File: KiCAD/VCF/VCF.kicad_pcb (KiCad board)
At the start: 2 copper layers, 50 x 100 mm, 50 parts, among them J1 FM, J2 CV, J3 IN, J4 OUT, J5 Conn_01x03, J6 Conn_01x03, Q1 2N3904, SW1 SW_SPDT, SW2 SW_SPDT, U1 TL072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

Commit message: VCF PCB Start
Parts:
- moved R17 115.8 mm to (172.4, 70.0)
- moved R26 115.3 mm to (190.0, 81.0)
- moved R27 115.3 mm to (190.0, 85.0)
- moved R18 109.6 mm to (162.4, 70.0)
- moved U1 108.2 mm to (165.0, 110.0)
- moved R25 107.1 mm to (187.4, 95.0)
- moved R24 102.9 mm to (185.0, 100.0)
- moved SW2 102.0 mm to (190.0, 70.0)
- moved R19 100.4 mm to (147.4, 70.0)
- moved R20 96.8 mm to (161.2, 102.0)
- moved J1 90.8 mm to (150.0, 60.0), turned to -90 degrees
- moved R23 89.7 mm to (172.0, 98.6), turned to 90 degrees
- moved SW1 84.3 mm to (105.0, 45.3)
- moved R15 80.9 mm to (146.4, 87.5)
- moved R21 79.7 mm to (161.4, 88.0)
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
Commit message: VCF PCB
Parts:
- added Ref**: Val**, HackSynth:PancakeLegend Logo - 10mm, B.Cu at (194.5, 77.8)
- added Ref**: Val**, HackSynth:CCHS Logo - 10mm, B.Cu at (194.0, 62.2)
- moved R10 100.1 mm to (138.8, 55.5), turned to 180 degrees
- moved R16 98.7 mm to (168.8, 111.8), turned to 180 degrees
- moved R9 91.9 mm to (146.2, 144.8)
- moved C1 88.8 mm to (157.5, 125.0), turned to 90 degrees
- moved R3 86.3 mm to (146.2, 85.0)
- moved R11 86.3 mm to (138.8, 133.8), turned to 180 degrees
- moved R14 86.0 mm to (153.8, 115.0), turned to 180 degrees
- moved R12 86.0 mm to (138.8, 137.2), turned to 180 degrees
- moved R8 85.0 mm to (142.5, 88.7), turned to -90 degrees
- moved R7 84.2 mm to (143.0, 118.7), turned to -90 degrees
- moved R5 80.9 mm to (138.8, 115.0), turned to 180 degrees
- moved R2 80.2 mm to (138.8, 70.0), turned to 180 degrees
- moved R13 76.3 mm to (146.2, 100.0)
- moved R1 71.4 mm to (131.2, 85.0)
- moved R6 71.3 mm to (131.2, 100.0)
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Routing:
- net VSS: track 0.00 -> 139.1 mm
- net Net-(U3-+): track 0.00 -> 107.6 mm
- net Net-(SW1-B): track 0.00 -> 100.7 mm
- net Net-(D1-A): track 0.00 -> 93.2 mm, vias 0 -> 1
- net Net-(Q1-B): track 0.00 -> 83.4 mm, vias 0 -> 1
- net Net-(U4-+): track 0.00 -> 82.0 mm
- net Net-(Q1-E): track 0.00 -> 52.5 mm
- net Net-(U5B-+): track 0.00 -> 48.6 mm
- net Net-(J1-PadT): track 0.00 -> 37.4 mm
- net Net-(R25-Pad1): track 0.00 -> 36.8 mm
- net Net-(J2-PadT): track 0.00 -> 35.8 mm
- net Net-(U1B--): track 0.00 -> 35.3 mm, vias 0 -> 1
- net Net-(R3-Pad1): track 0.00 -> 33.7 mm
- net Net-(C2-Pad1): track 0.00 -> 32.5 mm
- net Net-(U5A-+): track 0.00 -> 30.6 mm
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- added copper zone on B.Cu, net VDD
- removed copper zone on B.Cu, net GND
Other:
- board text added: "PancakeLegend 2025"
- board text added: "VCF v1-0"

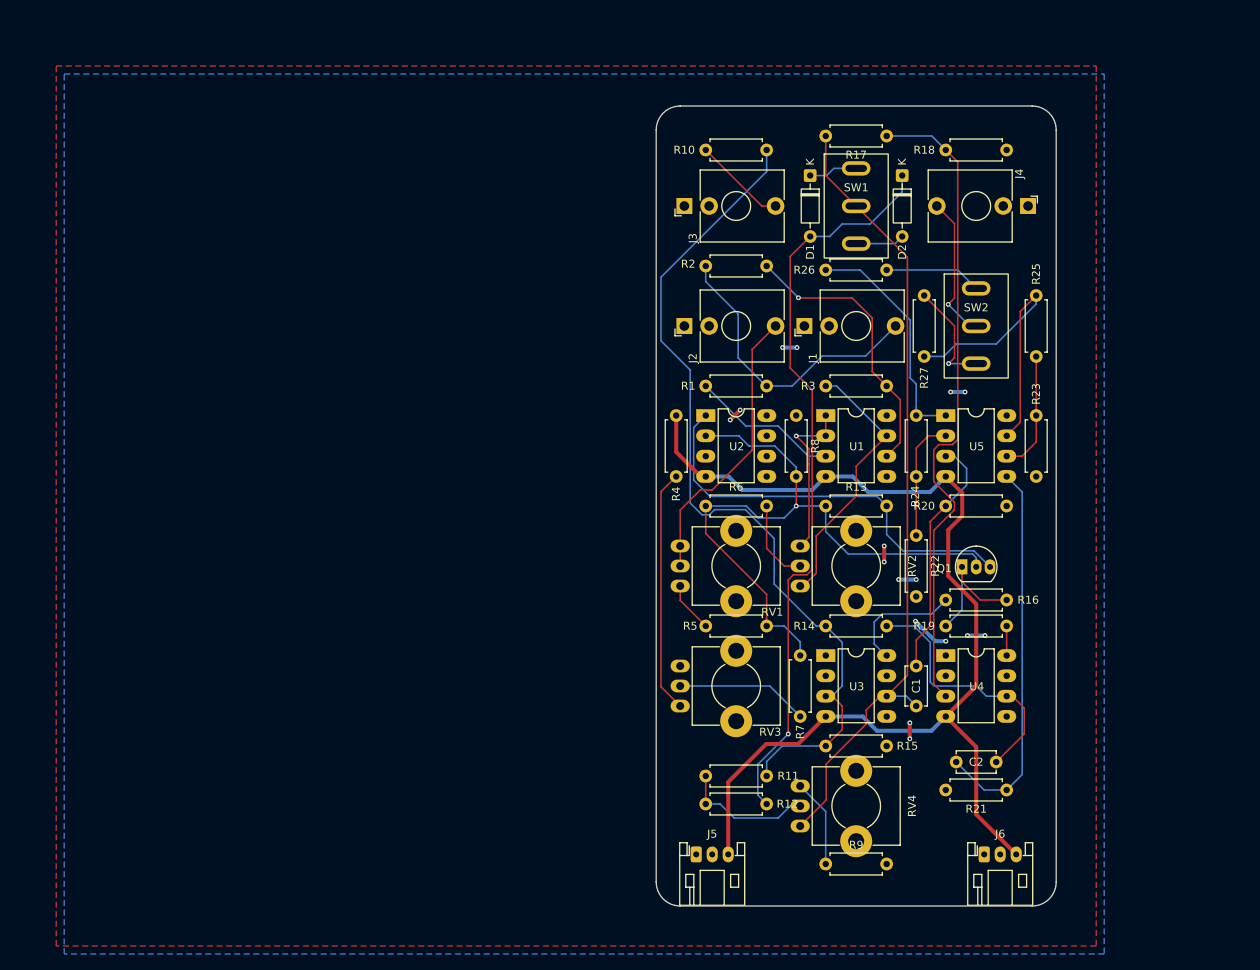
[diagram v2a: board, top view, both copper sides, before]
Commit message: MIDI to CV Cap Footprint Change
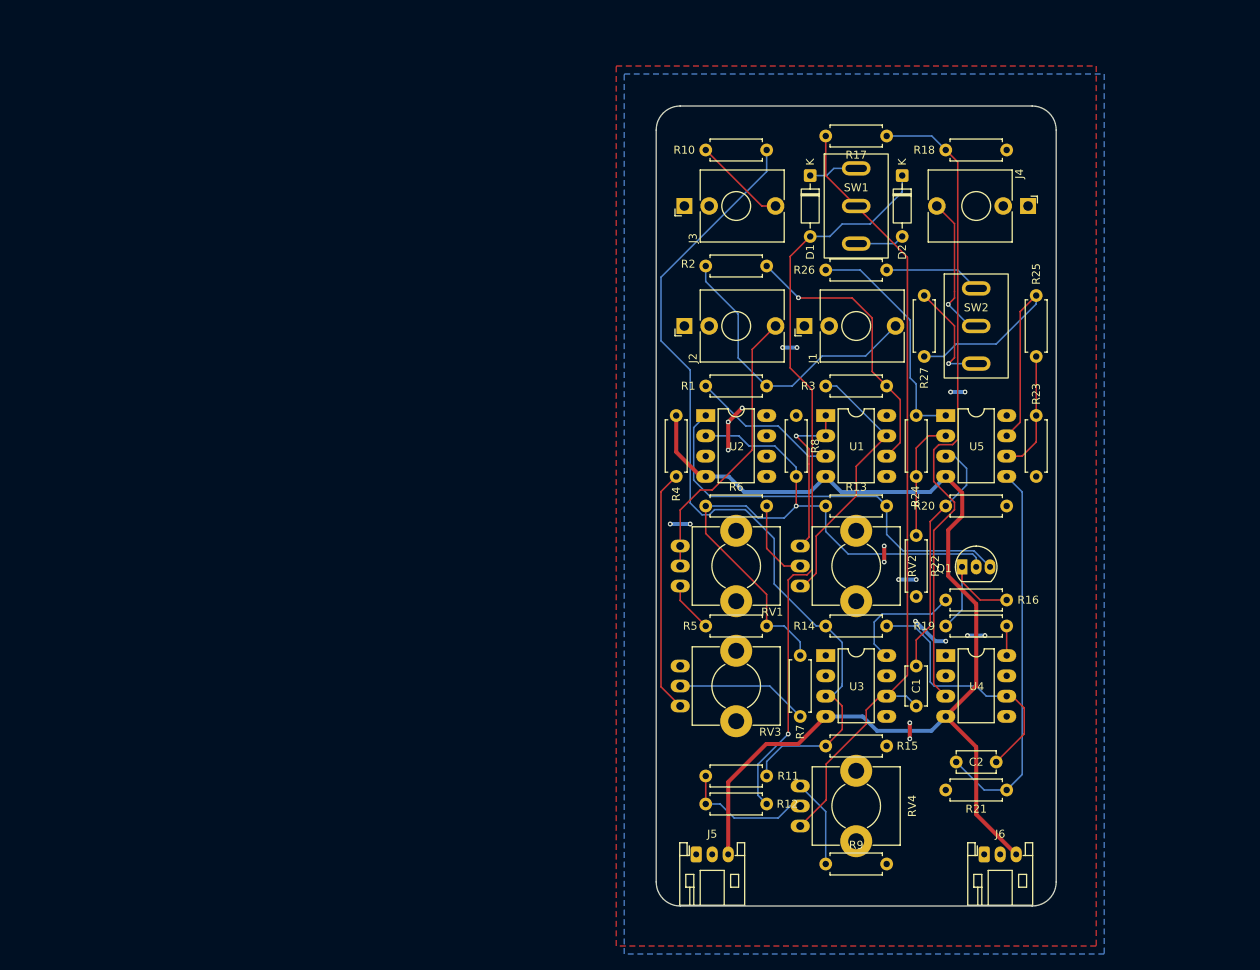
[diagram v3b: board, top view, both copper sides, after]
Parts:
- moved Ref** 4.78 mm to (194.0, 73.0)
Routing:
- net VDD: track 5.77 -> 9.97 mm, vias 6 -> 7
- net GND: track 12.8 -> 15.3 mm, vias 10 -> 12
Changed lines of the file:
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@@
 	(footprint "HackSynth:PancakeLegend Logo - 10mm"
 		(layer "B.Cu")
-		(at 194.5 77.75 180)
+		(at 194 73 180)
 		(property "Reference" "Ref**"
 			(at 0 0 0)
@@
 	)
 	(via
+		(at 129.25 102.25)
+		(size 0.6)
+		(drill 0.3)
+		(layers "F.Cu" "B.Cu")
+		(free yes)
+		(net 8)
+	)
+	(via
+		(at 126.75 102.25)
+		(size 0.6)
+		(drill 0.3)
+		(layers "F.Cu" "B.Cu")
+		(free yes)
+		(net 8)
+	)
+	(via
 		(at 163.9 116.2)
 		(size 0.6)
@@
 	)
 	(segment
+		(start 126.75 102.25)
+		(end 129.25 102.25)
+		(width 0.5)
+		(layer "B.Cu")
+		(net 8)
+	)
+	(segment
 		(start 161.2 116.9)
 		(end 159.9 116.9)
@@
 	)
 	(segment
-		(start 135.75 98)
-		(end 144.5 98)
+		(start 146.19 96.31)
+		(end 148.13 98.25)
+		(width 0.5)
+		(layer "B.Cu")
+		(net 13)
+	)
+	(segment
+		(start 159.25 98.25)
+		(end 161.19 96.31)
+		(width 0.5)
+		(layer "B.Cu")
+		(net 13)
+	)
+	(segment
+		(start 136 98.25)
+		(end 134.06 96.31)
 		(width 0.5)
 		(layer "B.Cu")
@@
 	)
 	(segment
-		(start 144.5 98)
-		(end 146.19 96.31)
-		(width 0.5)
-		(layer "B.Cu")
-		(net 13)
-	)
-	(segment
-		(start 149.56 96.31)
-		(end 151.5 98.25)
-		(width 0.5)
-		(layer "B.Cu")
-		(net 13)
-	)
-	(segment
 		(start 152.6 128.1)
 		(end 159.4 128.1)
@@
 	)
 	(segment
-		(start 159.25 98.25)
-		(end 161.19 96.31)
+		(start 134.06 96.31)
+		(end 131.19 96.31)
 		(width 0.5)
 		(layer "B.Cu")
@@
 	)
 	(segment
-		(start 134.06 96.31)
-		(end 135.75 98)
+		(start 146.19 96.31)
+		(end 144.25 98.25)
 		(width 0.5)
 		(layer "B.Cu")
@@
 	)
 	(segment
-		(start 131.19 96.31)
-		(end 134.06 96.31)
+		(start 148.13 98.25)
+		(end 159.25 98.25)
 		(width 0.5)
 		(layer "B.Cu")
@@
 	)
 	(segment
-		(start 146.19 96.31)
-		(end 149.56 96.31)
-		(width 0.5)
-		(layer "B.Cu")
-		(net 13)
-	)
-	(segment
-		(start 151.5 98.25)
-		(end 159.25 98.25)
+		(start 144.25 98.25)
+		(end 136 98.25)
 		(width 0.5)
 		(layer "B.Cu")
@@
 	)
 	(segment
+		(start 135.75 87.75)
+		(end 134 89.5)
+		(width 0.5)
+		(layer "F.Cu")
+		(net 14)
+	)
+	(segment
 		(start 156.7 127.1)
 		(end 156.7 129.1)
@@
 	)
 	(segment
-		(start 135.5 88)
-		(end 134.25 89.25)
-		(width 0.5)
-		(layer "F.Cu")
+		(start 134 93)
+		(end 134 89.5)
+		(width 0.5)
+		(layer "F.Cu")
+		(net 14)
+	)
+	(via
+		(at 134 93)
+		(size 0.6)
+		(drill 0.3)
+		(layers "F.Cu" "B.Cu")
+		(free yes)
 		(net 14)
 	)
@@
 	)
 	(via
-		(at 135.5 88)
+		(at 135.75 87.75)
 		(size 0.6)
 		(drill 0.3)
@@
 	)
 	(via
-		(at 134.25 89.25)
+		(at 134 89.5)
 		(size 0.6)
 		(drill 0.3)
@@
 		(polygon
 			(pts
-				(xy 50 45) (xy 180 45) (xy 180 155) (xy 50 155)
+				(xy 120 45) (xy 180 45) (xy 180 155) (xy 120 155)
 			)
 		)
@@
 		(polygon
 			(pts
-				(xy 51 46) (xy 181 46) (xy 181 156) (xy 51 156)
+				(xy 121 46) (xy 181 46) (xy 181 156) (xy 121 156)
 			)
 		)

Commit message: VCF PCB
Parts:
- removed SW1, SW2: SW_SPDT, HackSynth:Switch SPDT - MTS-102
- added HARD/SOFT1: SW_SPDT, HackSynth:Switch SPDT - MTS-102, F.Cu at (165.0, 92.5)
- added LP/BP1: SW_SPDT, HackSynth:Switch SPDT - MTS-102, F.Cu at (150.0, 92.5)
- added REF**: Untitled, HackSynth:Module 50x100mm, F.Cu at (70.0, 100.0)
- RV1: value 100k -> R_Trim 100k; footprint HackSynth:Potentiometer_Alps_RK09K_Horizontal -> HackSynth:TrimPot_Bourns_3339S_Horizontal
- moved Ref** 98.0 mm to (140.9, 144.5)
- moved Ref** 79.0 mm to (159.5, 144.1)
- moved R5 56.4 mm to (142.5, 58.7), turned to -90 degrees
- moved R24 50.9 mm to (131.2, 132.2), turned to 0 degrees
- moved R11 50.8 mm to (146.1, 83.5), turned to 0 degrees
- moved R25 47.7 mm to (157.5, 118.9)
- moved R16 47.3 mm to (127.5, 88.7), turned to -90 degrees
- moved R12 45.0 mm to (157.5, 96.3), turned to 90 degrees
- moved R14 42.7 mm to (127.5, 81.3), turned to 90 degrees
- moved D2 42.4 mm to (160.9, 100.8), turned to 0 degrees
- moved R23 37.2 mm to (146.2, 115.0), turned to 0 degrees
- moved R22 37.1 mm to (138.8, 135.8), turned to 180 degrees
- moved D1 35.6 mm to (168.8, 84.5), turned to 180 degrees
- moved R27 34.0 mm to (142.5, 111.3)
- moved Q1 33.6 mm to (133.7, 92.5)
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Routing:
- net Net-(D1-A): track 93.2 -> 20.6 mm
- net Net-(Q1-B): track 83.4 -> 135.9 mm, vias 1 -> 2
- net Net-(R11-Pad2): track 16.7 -> 67.8 mm
- net Net-(U4-+): track 82.0 -> 55.6 mm, vias 0 -> 2
- net Net-(J2-PadT): track 35.8 -> 11.1 mm
- net Net-(R24-Pad1): track 29.1 -> 51.5 mm, vias 0 -> 1
- net Net-(U1A-+): track 18.6 -> 37.7 mm, vias 0 -> 2
- net Net-(U5B-+): track 48.6 -> 30.4 mm
- net Net-(C2-Pad1): track 32.5 -> 50.5 mm, vias 0 -> 2
- net Net-(R4-Pad1): track 30.5 -> 12.7 mm, vias 0 -> 1
- net Net-(LP/BP1-B): track 18.2 -> 35.0 mm, vias 1 -> 0
- net Net-(Q1-E): track 52.5 -> 37.1 mm, vias 0 -> 1
- net Net-(R25-Pad1): track 36.8 -> 21.7 mm
- net Net-(HARD/SOFT1-B): track 100.7 -> 88.4 mm, vias 0 -> 2
- net Net-(U3-Set): track 15.0 -> 27.1 mm, vias 0 -> 1
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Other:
- board text added: "BP/LP"
- board text added: "CV"
- board text added: "FM"
- board text added: "FREQ"
- board text added: "HARD"
- board text added: "IN"
- board text added: "JACK"
- board text added: "KNOB"
- board text added: "OUT"
- board text added: "RES"
- board text added: "SWITCH"
- board text added: "TRIM"
- board text added: "VCF v1-0 - PancakeLegend 2025"
- board text removed: "PancakeLegend 2025"
- board text removed: "VCF v1-0"

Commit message: VCF Reorg
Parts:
- removed the REF** at (70.0, 100.0)
- moved R15 54.6 mm to (172.5, 96.3), turned to 90 degrees
- moved R7 48.9 mm to (161.2, 139.2), turned to 0 degrees
- moved R4 45.0 mm to (172.5, 118.7)
- moved C1 36.1 mm to (172.5, 105.0), turned to -90 degrees
- moved R3 33.5 mm to (142.5, 118.7)
- moved RV2 33.5 mm to (135.0, 107.5)
- moved RV3 33.5 mm to (165.0, 122.5)
- moved U1 33.5 mm to (135.0, 122.5)
- moved U3 33.5 mm to (165.0, 107.5)
- moved R9 22.4 mm to (138.8, 139.2), turned to 180 degrees
- moved R6 19.0 mm to (127.5, 126.3), turned to 90 degrees
- moved R11 0.75 mm to (146.1, 84.2)
- moved D2 0.25 mm to (161.2, 100.8)
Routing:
- net Net-(U3-Set): track 27.1 -> 54.8 mm, vias 1 -> 0
- net Net-(U1A--): track 29.7 -> 7.27 mm, vias 1 -> 0
- net Net-(U1B--): track 38.0 -> 60.1 mm, vias 2 -> 0
- net Net-(R3-Pad1): track 31.5 -> 13.5 mm
- net Net-(Q1-B): track 135.9 -> 153.5 mm, vias 2 -> 1
- net VSS: track 146.7 -> 161.6 mm
- net Net-(U1A-+): track 37.7 -> 47.1 mm, vias 2 -> 0
- net Net-(HARD/SOFT1-B): track 88.4 -> 96.3 mm, vias 2 -> 1
- net Net-(U5A-+): track 26.0 -> 33.3 mm
- net Net-(U3-+): track 106.1 -> 99.6 mm, vias 1 -> 0
- net Net-(R9-Pad1): track 18.3 -> 11.9 mm
- net Net-(R6-Pad2): track 15.0 -> 10.3 mm
- net Net-(R7-Pad2): track 9.85 -> 11.3 mm
- net Net-(C2-Pad1): track 50.5 -> 49.1 mm, vias 2 -> 1
- net GND: track 7.36 -> 6.13 mm
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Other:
- board text removed: "JACK"
- board text removed: "KNOB"
- board text removed: "SWITCH"

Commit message: VCF Gerbers
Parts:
- moved R11 15.5 mm to (157.5, 73.7), turned to -90 degrees
- moved R2 11.7 mm to (146.2, 84.2), turned to 0 degrees
- moved R10 7.62 mm to (127.5, 66.3), turned to 90 degrees
- moved R23 7.62 mm to (153.8, 115.0), turned to 180 degrees
- renumbered LP/BP1 to LP/BP, HARD/SOFT1 to SOFT/HARD
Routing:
- net Net-(U1B--): track 60.1 -> 49.4 mm
- net Net-(U3-+): track 99.6 -> 91.9 mm, vias 0 -> 1
- net VSS: track 161.6 -> 168.3 mm
- net Net-(J3-PadT): track 7.96 -> 13.1 mm
- net Net-(J1-PadT): track 34.6 -> 30.3 mm
- net Net-(Q1-E): track 37.1 -> 41.4 mm
- net Net-(U5B--): track 20.9 -> 17.2 mm, vias 1 -> 0
- net GND: track 6.13 -> 2.94 mm, vias 2 -> 1
- net Net-(R25-Pad1): track 21.8 -> 23.3 mm
- net Net-(R11-Pad2): track 66.7 -> 67.9 mm
- net Net-(U4-+): track 55.6 -> 56.8 mm
- net Net-(R4-Pad1): track 12.9 -> 13.9 mm
- net Net-(U3-Set): track 54.8 -> 53.8 mm
- net Net-(D2-A): track 6.19 -> 5.28 mm
- net Net-(R3-Pad1): track 13.5 -> 12.8 mm
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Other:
- board text added: "VCF"
- board text removed: "BP/LP"
- board text removed: "HARD"
- board text removed: "TRIM"
